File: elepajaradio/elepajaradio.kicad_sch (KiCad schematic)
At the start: 29 parts, among them J1 SPI, J2 UART, J3 vdd_gnd, J4 reset, SW1 RotaryEncoder, SW2 SW_Push, SW3 SW_Push, U1 MAX2606, U2 OLED_I2C, U3 ATmega328PB-A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

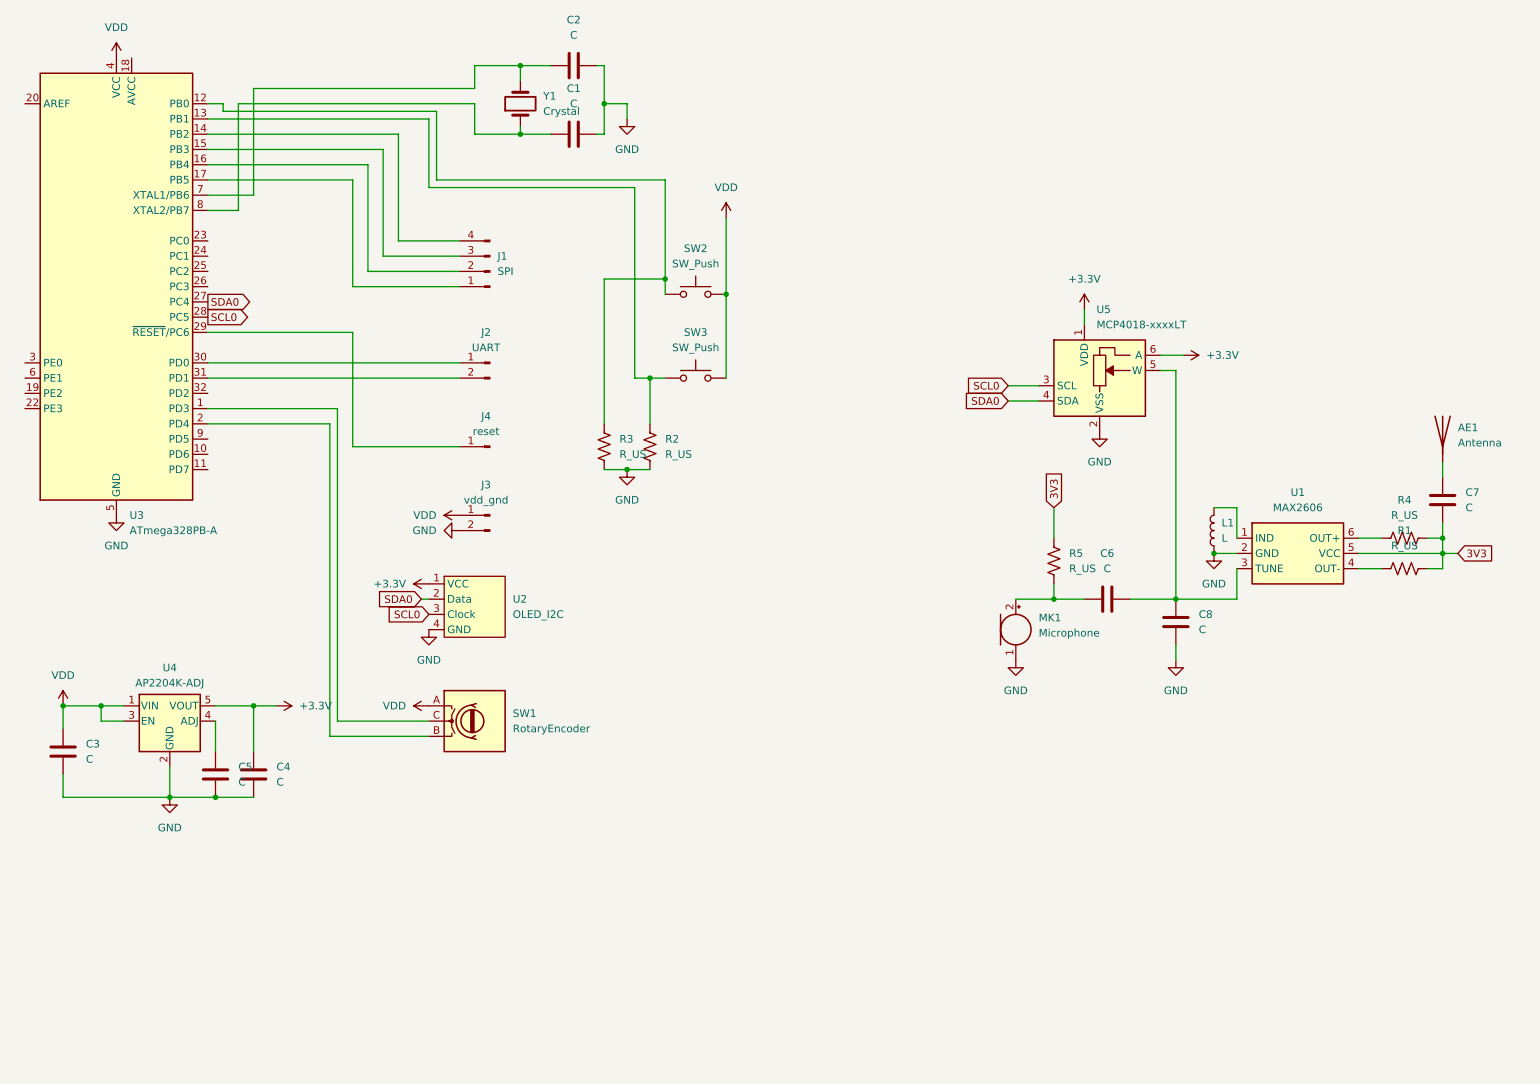
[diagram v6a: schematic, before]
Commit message: sized transmission line v2
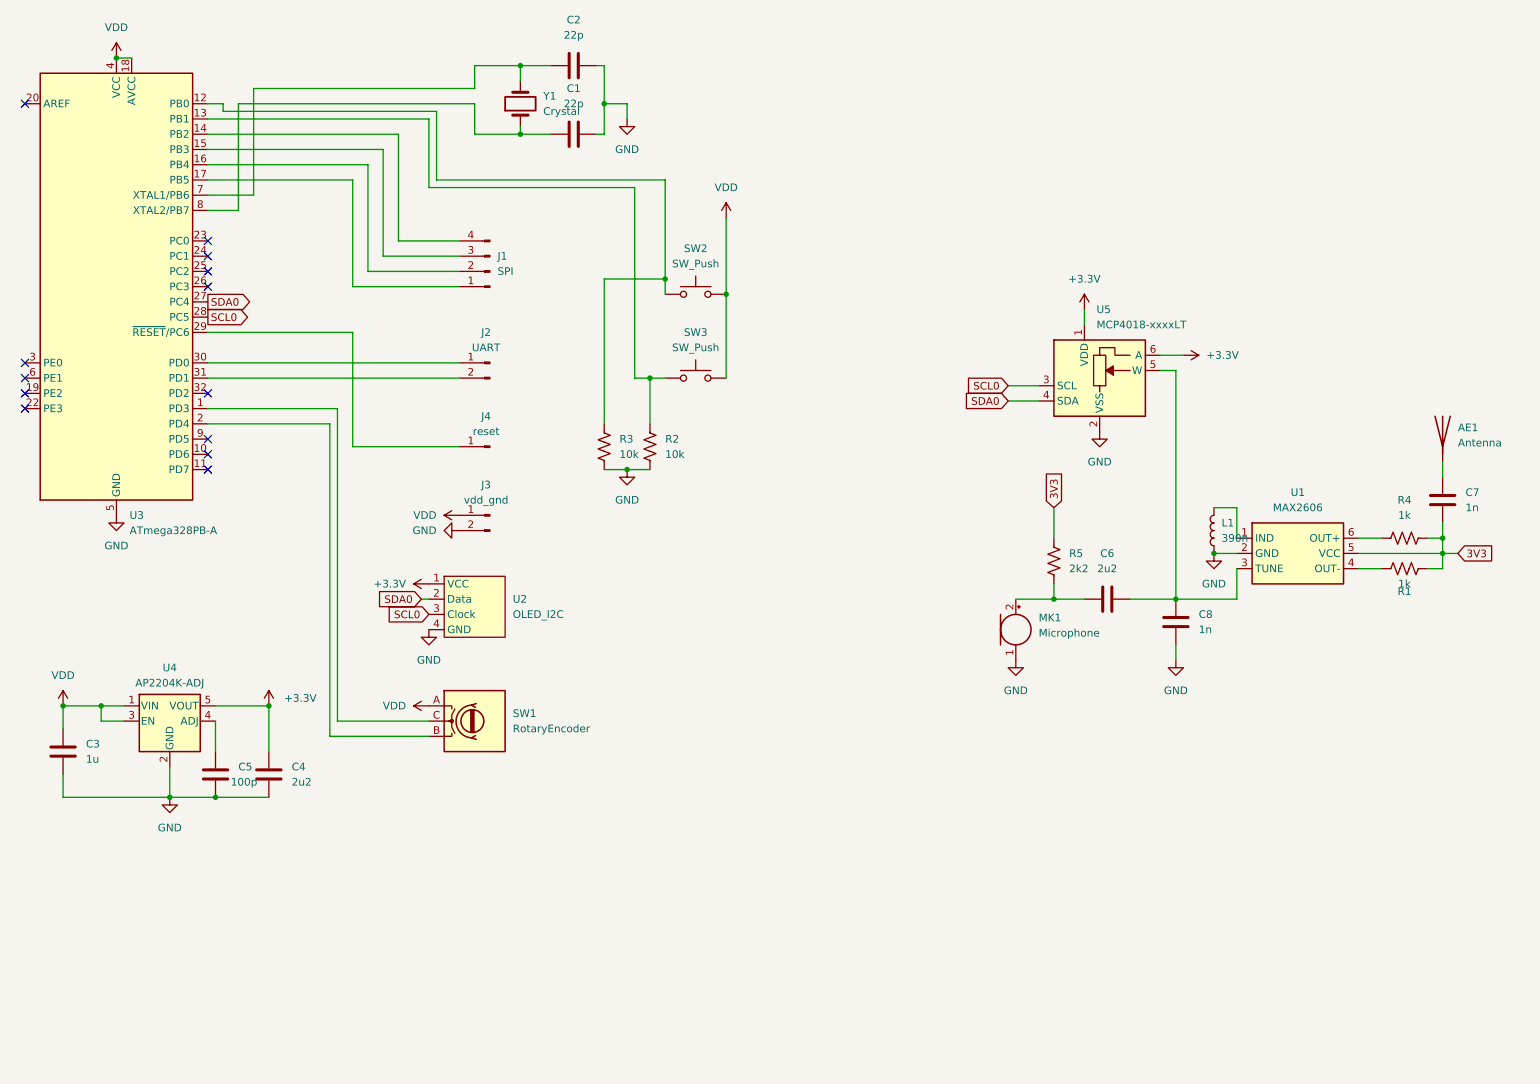
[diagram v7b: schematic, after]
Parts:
- C1, C2: value C -> 22p
- C3: value C -> 1u
- C4, C6: value C -> 2u2
- C5: value C -> 100p
- C7, C8: value C -> 1n
- L1: value L -> 390n
- R1, R4: value R_US -> 1k
- R2, R3: value R_US -> 10k
- R5: value R_US -> 2k2
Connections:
- net VDD: now also U3.18 (AVCC)
- no-connect marks 0 -> 13
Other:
- moved on the sheet: C4
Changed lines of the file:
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@@
   (junction (at 97.79 25.4) (diameter 0) (color 0 0 0 0)
   )
+  (junction (at 30.48 24.13) (diameter 0) (color 0 0 0 0)
+  )
   (junction (at 97.79 36.83) (diameter 0) (color 0 0 0 0)
   )
@@
   (junction (at 186.69 114.3) (diameter 0) (color 0 0 0 0)
   )
-  (junction (at 53.34 132.08) (diameter 0) (color 0 0 0 0)
-  )
+  (junction (at 55.88 132.08) (diameter 0) (color 0 0 0 0)
+  )
+  (no_connect (at 45.72 80.01))
+  (no_connect (at 15.24 82.55))
+  (no_connect (at 45.72 59.69))
+  (no_connect (at 15.24 31.75))
+  (no_connect (at 45.72 92.71))
+  (no_connect (at 15.24 74.93))
+  (no_connect (at 15.24 80.01))
+  (no_connect (at 45.72 87.63))
+  (no_connect (at 45.72 57.15))
+  (no_connect (at 45.72 62.23))
+  (no_connect (at 15.24 77.47))
+  (no_connect (at 45.72 54.61))
+  (no_connect (at 45.72 90.17))
   (wire (pts (xy 97.79 27.94) (xy 97.79 25.4))
     (stroke (width 0) (type default))
@@
     (stroke (width 0) (type default))
   )
+  (wire (pts (xy 30.48 24.13) (xy 33.02 24.13))
+    (stroke (width 0) (type default))
+  )
   (wire (pts (xy 213.36 99.06) (xy 217.17 99.06))
     (stroke (width 0) (type default))
@@
     (stroke (width 0) (type default))
   )
-  (wire (pts (xy 46.99 147.32) (xy 53.34 147.32))
+  (wire (pts (xy 46.99 147.32) (xy 55.88 147.32))
     (stroke (width 0) (type default))
   )
@@
     (stroke (width 0) (type default))
   )
-  (wire (pts (xy 53.34 132.08) (xy 46.99 132.08))
+  (wire (pts (xy 46.99 132.08) (xy 55.88 132.08))
     (stroke (width 0) (type default))
   )
@@
     (stroke (width 0) (type default))
   )
-  (wire (pts (xy 53.34 132.08) (xy 53.34 139.7))
+  (wire (pts (xy 55.88 132.08) (xy 55.88 139.7))
     (stroke (width 0) (type default))
   )
@@
   )
   (wire (pts (xy 67.31 82.55) (xy 67.31 134.62))
-    (stroke (width 0) (type default))
-  )
-  (wire (pts (xy 57.15 132.08) (xy 53.34 132.08))
     (stroke (width 0) (type default))
   )
@@
     )
   )
-  (symbol (lib_id "power:+3.3V") (at 57.15 132.08 270) (unit 1)
-    (in_bom yes) (on_board yes) (dnp no) (fields_autoplaced)
-    (property "Reference" "#PWR07" (at 53.34 132.08 0)
-      (effects (font (size 1.27 1.27)) hide)
-    )
-    (property "Value" "+3.3V" (at 60.96 132.08 90)
-      (effects (font (size 1.27 1.27)) (justify left))
-    )
-    (property "Footprint" "" (at 57.15 132.08 0)
-      (effects (font (size 1.27 1.27)) hide)
-    )
-    (property "Datasheet" "" (at 57.15 132.08 0)
+  (symbol (lib_id "power:+3.3V") (at 55.88 132.08 0) (unit 1)
+    (in_bom yes) (on_board yes) (dnp no) (fields_autoplaced)
+    (property "Reference" "#PWR07" (at 55.88 135.89 0)
+      (effects (font (size 1.27 1.27)) hide)
+    )
+    (property "Value" "+3.3V" (at 58.42 130.81 0)
+      (effects (font (size 1.27 1.27)) (justify left))
+    )
+    (property "Footprint" "" (at 55.88 132.08 0)
+      (effects (font (size 1.27 1.27)) hide)
+    )
+    (property "Datasheet" "" (at 55.88 132.08 0)
       (effects (font (size 1.27 1.27)) hide)
     )
@@
     )
   )
-  (symbol (lib_id "Device:C") (at 53.34 143.51 0) (unit 1)
-    (in_bom yes) (on_board yes) (dnp no) (fields_autoplaced)
-    (property "Reference" "C4" (at 57.15 142.2399 0)
-      (effects (font (size 1.27 1.27)) (justify left))
-    )
-    (property "Value" "C" (at 57.15 144.7799 0)
-      (effects (font (size 1.27 1.27)) (justify left))
-    )
-    (property "Footprint" "Capacitor_SMD:C_0603_1608Metric" (at 54.3052 147.32 0)
-      (effects (font (size 1.27 1.27)) hide)
-    )
-    (property "Datasheet" "~" (at 53.34 143.51 0)
+  (symbol (lib_id "Device:C") (at 55.88 143.51 0) (unit 1)
+    (in_bom yes) (on_board yes) (dnp no) (fields_autoplaced)
+    (property "Reference" "C4" (at 59.69 142.2399 0)
+      (effects (font (size 1.27 1.27)) (justify left))
+    )
+    (property "Value" "2u2" (at 59.69 144.7799 0)
+      (effects (font (size 1.27 1.27)) (justify left))
+    )
+    (property "Footprint" "Capacitor_SMD:C_0603_1608Metric" (at 56.8452 147.32 0)
+      (effects (font (size 1.27 1.27)) hide)
+    )
+    (property "Datasheet" "~" (at 55.88 143.51 0)
       (effects (font (size 1.27 1.27)) hide)
     )
@@
       (effects (font (size 1.27 1.27)) (justify left))
     )
-    (property "Value" "C" (at 255.27 99.0599 0)
+    (property "Value" "1n" (at 255.27 99.0599 0)
       (effects (font (size 1.27 1.27)) (justify left))
     )
@@
       (effects (font (size 1.27 1.27)) (justify left))
     )
-    (property "Value" "C" (at 25.4 140.9699 0)
+    (property "Value" "1u" (at 25.4 140.9699 0)
       (effects (font (size 1.27 1.27)) (justify left))
     )
@@
       (effects (font (size 1.27 1.27)))
     )
-    (property "Value" "C" (at 106.68 20.32 90)
+    (property "Value" "22p" (at 106.68 20.32 90)
       (effects (font (size 1.27 1.27)))
     )
@@
   )
   (symbol (lib_id "Device:R_US") (at 245.11 109.22 270) (unit 1)
-    (in_bom yes) (on_board yes) (dnp no) (fields_autoplaced)
-    (property "Reference" "R1" (at 245.11 102.87 90)
-      (effects (font (size 1.27 1.27)))
-    )
-    (property "Value" "R_US" (at 245.11 105.41 90)
+    (in_bom yes) (on_board yes) (dnp no)
+    (property "Reference" "R1" (at 245.11 113.03 90)
+      (effects (font (size 1.27 1.27)))
+    )
+    (property "Value" "1k" (at 245.11 111.76 90)
       (effects (font (size 1.27 1.27)))
     )
@@
       (effects (font (size 1.27 1.27)) (justify right))
     )
-    (property "Value" "R_US" (at 189.23 109.2199 0)
+    (property "Value" "2k2" (at 189.23 109.2199 0)
       (effects (font (size 1.27 1.27)) (justify right))
     )
@@
       (effects (font (size 1.27 1.27)))
     )
-    (property "Value" "R_US" (at 245.11 100.33 90)
+    (property "Value" "1k" (at 245.11 100.33 90)
       (effects (font (size 1.27 1.27)))
     )
@@
   )
   (symbol (lib_id "Device:C") (at 46.99 143.51 0) (unit 1)
-    (in_bom yes) (on_board yes) (dnp no) (fields_autoplaced)
-    (property "Reference" "C5" (at 50.8 142.2399 0)
-      (effects (font (size 1.27 1.27)) (justify left))
-    )
-    (property "Value" "C" (at 50.8 144.7799 0)
+    (in_bom yes) (on_board yes) (dnp no)
+    (property "Reference" "C5" (at 50.8 142.24 0)
+      (effects (font (size 1.27 1.27)) (justify left))
+    )
+    (property "Value" "100p" (at 49.53 144.78 0)
       (effects (font (size 1.27 1.27)) (justify left))
     )
@@
       (effects (font (size 1.27 1.27)))
     )
-    (property "Value" "C" (at 106.68 31.75 90)
+    (property "Value" "22p" (at 106.68 31.75 90)
       (effects (font (size 1.27 1.27)))
     )
@@
       (effects (font (size 1.27 1.27)) (justify right))
     )
-    (property "Value" "R_US" (at 121.92 90.1699 0)
+    (property "Value" "10k" (at 121.92 90.1699 0)
       (effects (font (size 1.27 1.27)) (justify right))
     )
@@
       (effects (font (size 1.27 1.27)) (justify left))
     )
-    (property "Value" "C" (at 210.82 119.3799 0)
+    (property "Value" "1n" (at 210.82 119.3799 0)
       (effects (font (size 1.27 1.27)) (justify left))
     )
@@
       (effects (font (size 1.27 1.27)) (justify right))
     )
-    (property "Value" "R_US" (at 114.3 90.1699 0)
+    (property "Value" "10k" (at 114.3 90.1699 0)
       (effects (font (size 1.27 1.27)) (justify right))
     )
@@
       (effects (font (size 1.27 1.27)) (justify right))
     )
-    (property "Value" "L" (at 214.63 104.1399 0)
+    (property "Value" "390n" (at 214.63 104.1399 0)
       (effects (font (size 1.27 1.27)) (justify right))
     )
@@
       (effects (font (size 1.27 1.27)))
     )
-    (property "Value" "C" (at 195.58 109.22 90)
-      (effects (font (size 1.27 1.27)))
-    )
+    (property "Value" "2u2" (at 195.58 109.22 90)
+      (effects (font (size 1.27 1.27)))
+    )

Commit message: fixes on new branch for 3v3 node
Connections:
- net +3.3V is gone; now on net 3V3: C4.1, U2.1 (VCC), U4.5 (VOUT), U5.1 (VDD), U5.6 (A)
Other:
- moved on the sheet: AE1, C6, C7, C8, L1, MK1, R1, R4, R5, U1, U5
